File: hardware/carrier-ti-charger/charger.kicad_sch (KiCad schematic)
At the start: 16 parts, among them J2 J_NTC 100k ENTC-EB-100K4262-02, U4 MAX77757JEFG420+T

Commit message: TI charger
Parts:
- removed C34, C7: 2.2u 25V X7R, Capacitor_SMD:C_0603_1608Metric, symbol Device:C
- removed R37, R6: 6.2k 1%, Resistor_SMD:R_0603_1608Metric, symbol Device:R
- removed R8: 154k 1%, Resistor_SMD:R_0603_1608Metric, symbol Device:R
- removed U4: MAX77757JEFG420+T, carrier:FC2QFN-24_L3.0-W3.0-P0.40_MAX77757, symbol carrier:MAX77757JEFG420
- added C41, C42, C47: 10u 25V X7R, Capacitor_SMD:C_0805_2012Metric, symbol Device:C
- added C43, C44, C46, C50: 100n 50V, Capacitor_SMD:C_0603_1608Metric, symbol Device:C
- added C45: 47n 50V, Capacitor_SMD:C_0603_1608Metric, symbol Device:C
- added C48: 4.7u 16V X5R, Capacitor_SMD:C_0603_1608Metric, symbol Device:C
- added C49: 1n 50V, Capacitor_SMD:C_0603_1608Metric, symbol Device:C
- added Q10, Q12: 2N7002, Package_TO_SOT_SMD:SOT-23, symbol Transistor_FET:2N7002
- added R56: 4.7k 1%, Resistor_SMD:R_0603_1608Metric, symbol Device:R
- added R57, R63: 47k 1%, Resistor_SMD:R_0603_1608Metric, symbol Device:R
- added R58, R62, R64: 100k 1%, Resistor_SMD:R_0603_1608Metric, symbol Device:R
- added R59: 80.6k 1%, Resistor_SMD:R_0603_1608Metric, symbol Device:R
- added R60: 768k 1%, Resistor_SMD:R_0603_1608Metric, symbol Device:R
- added R61: 150R, Resistor_SMD:R_0603_1608Metric, symbol Device:R
- added R67, R68: 1M, Resistor_SMD:R_0603_1608Metric, symbol Device:R
- added TP8: CHG_INT_N, carrier:TestPoint_Pad_D1.5mm, symbol Connector:TestPoint
- added U14: LM73100RPWR, carrier:VQFN-10_L2.0-W2.0-P0.45-HR_LM73100, symbol carrier:LM73100RPW
- added U4: BQ25798RQMR, Package_DFN_QFN:Texas_RQM0029A_VQFN-29_4x4mm_P0.4mm, symbol Battery_Management:BQ25798
- C5: value 2.2u 25V X7R -> 100n 50V; LCSC C415535 -> C14663
- C8: value 100n -> 47n 50V; LCSC C14663 -> C1622
- L1: value 1uH FXL0630-1R0-M -> 2.2uH FXL0630-2R2-M; LCSC C167216 -> C167218
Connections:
- net BAT_TS: now also R59.1, R60.1, U4.16 (TS)
- net CHG_STAT_N: now also U4.1 (STAT)
- net GND: now also C41.2, C42.2, C43.2, C44.2, C46.2, C47.2, C48.2, C49.2, C50.2, Q10.2 (S), Q12.2 (S), R56.2, R58.2, R60.2, R64.2, R68.2, U14.2 (OVLO), U14.4 (PGTH), U14.8 (GND), U14.9 (IMON), U4.10 (ACDRV2), U4.11 (ACDRV1), U4.27 (GND)
- net USB_DN: now also U4.7 (D-)
- net USB_DP: now also U4.6 (D+)
- net USB_VBUS: now also C41.1, C42.1, C43.1, R63.1, U4.2 (VBUS), U4.3 (VBUS), U4.8 (VAC2), U4.9 (VAC1)
- net VBAT: now also C47.1, R61.2, U4.22 (BAT), U4.23 (BAT)
- net VSYS: now also C46.1, U4.25 (SYS); no longer L1.2
- net CHG_BTST renamed CHG_BTST1
- net CHG_BTST1: now also U4.4 (BTST1)
- net CHG_BYP renamed CHG_PMID
- net CHG_PMID: now also C44.1, C50.1, R67.1, U14.5 (IN), U4.29 (PMID)
- net CHG_SW renamed CHG_SW1
- net CHG_SW1: now also U4.28 (SW1)
- new net CHG_BATP: R61.1, U4.18 (BATP)
- new net CHG_BTST2: C45.1, U4.19 (BTST2)
- new net CHG_DIS: U4.13 (~{CE})
- new net CHG_ILIM: R57.2, R58.1, U4.17 (ILIM_HIZ)
- new net CHG_INT_N: R62.2, TP8.1, U4.21 (~{INT})
- new net CHG_PROG: R56.1, U4.20 (PROG)
- new net CHG_REGN: C48.1, R57.1, R59.2, U4.5 (REGN)
- new net CHG_SDRV: C49.1, U4.24 (SDRV)
- new net CHG_SW2: C45.2, L1.2, U4.26 (SW2)
- new net ESP_3V3: R62.1
- new net ESP_5V_D: U14.6 (OUT)
- new net ESP_PMID_EN: Q12.3 (D), R67.2, R68.1, U14.1 (EN/UVLO)
- new net I2C_SCL: U4.14 (SCL)
- new net I2C_SDA: U4.15 (SDA)
- new net SW_EN: Q12.1 (G)
- new net USB_G2: Q10.1 (G), R63.2, R64.1
- new net USB_OK_N: Q10.3 (D)
- no-connect marks 0 -> 4
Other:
- note added: "1 A default charge, ESP32-S3 raises ICHG over I2C, watchdog (40 s) falls back. CE from the thermostat path (CHG_DIS high = charging off). TREG default 120 C."
- note added: "Charger BQ25798, 1S, 5 V USB input"
- note added: "D+/D- BC1.2 on chip, CC has Rd only (USB input sheet). No ship FET: SDRV 1 nF, QON open. PROG 4.7k = 1S, 750 kHz. ILIM_HIZ 3.4 V = 3 A. TS 80.6k/768k: 3/43 C."
- note added: "Display feed in charger mode, from PMID:"
- note added: "Q12: slider on = U14 off, no handover on unplug."
- note added: "Red LED: USB present (Q10). Green LED: STAT, charging."
- note added: "inside the charger's input current limit."
- note removed: "Battery charger (MAX77757)"
- title: Charger MAX77757 -> Charger BQ25798
- moved on the sheet: C10, C11, C33, C35, C5, C6, C9, J2, L1

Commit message: Switch parts (BMP580, TPS259474L) due to stock shortage.
Also, add overvoltage (OVLO) protection.
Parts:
- added C55: 2.2n 50V, Capacitor_SMD:C_0603_1608Metric, symbol Device:C
- added R72: 1.65k, Resistor_SMD:R_0603_1608Metric, symbol Device:R
- added R77: 5.1k, carrier:R_0402_1005Metric_NoSilk, symbol Device:R
- added R78: 1.5k, carrier:R_0402_1005Metric_NoSilk, symbol Device:R
- U14: value LM73100RPWR -> TPS259474LRPWR; symbol carrier:LM73100RPW -> carrier:TPS259474LRPW; LCSC C3210761 -> C2864845
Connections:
- net CHG_PMID: now also R77.1
- net GND: now also C55.2, R72.2, R78.2; no longer U14.2 (OVLO), U14.9 (IMON)
- net U14_DVDT: now reaches U14.7 (DVDT)
- net U14_DVDT: now also C55.1
- new net U14_ILM: R72.1, U14.9 (ILM)
- new net U14_OVLO: R77.2, R78.1, U14.2 (OVLO)
- no-connect marks 4 -> 3

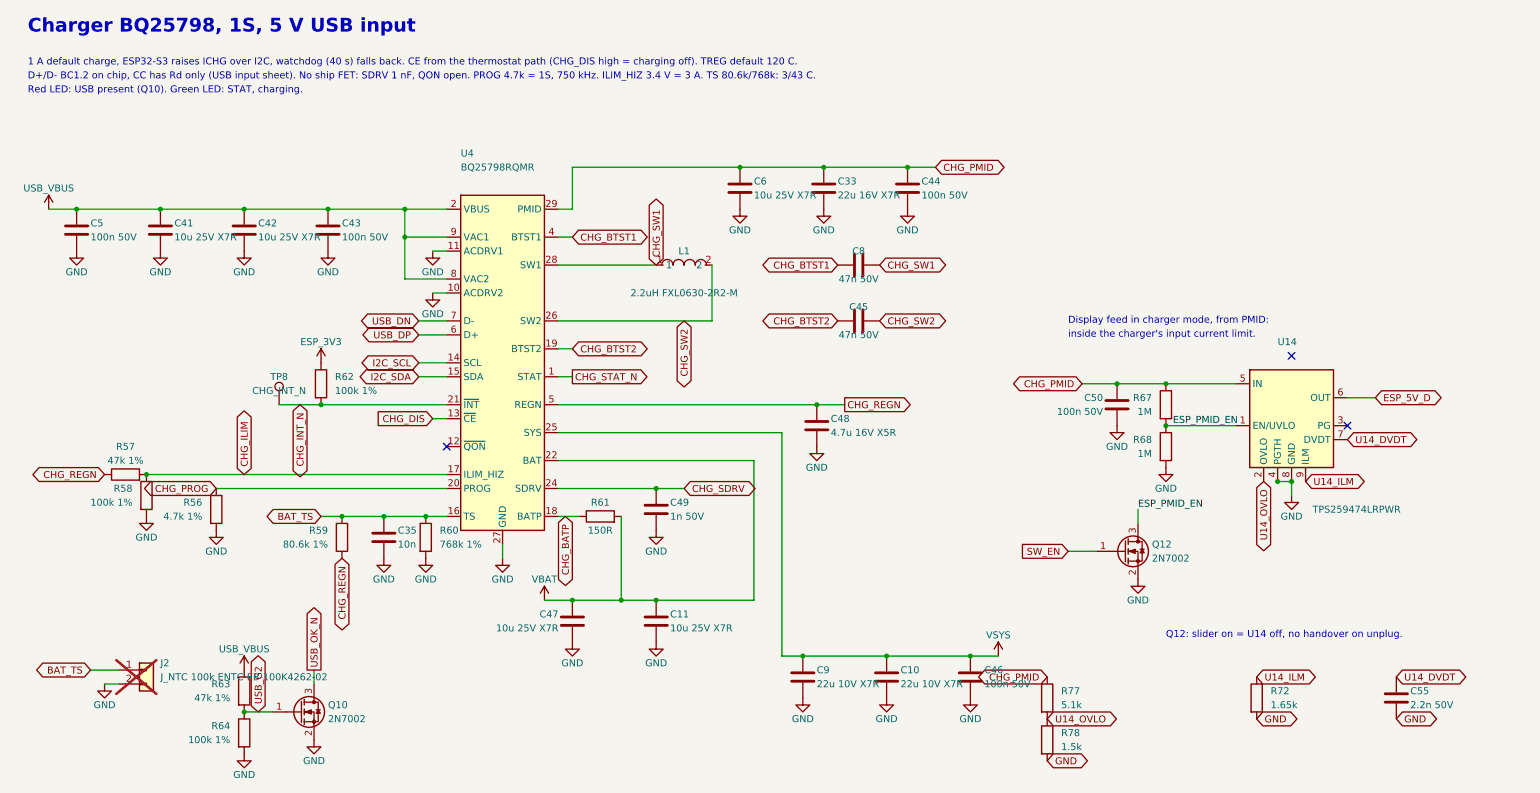
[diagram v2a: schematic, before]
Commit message: Add reset FET switch.
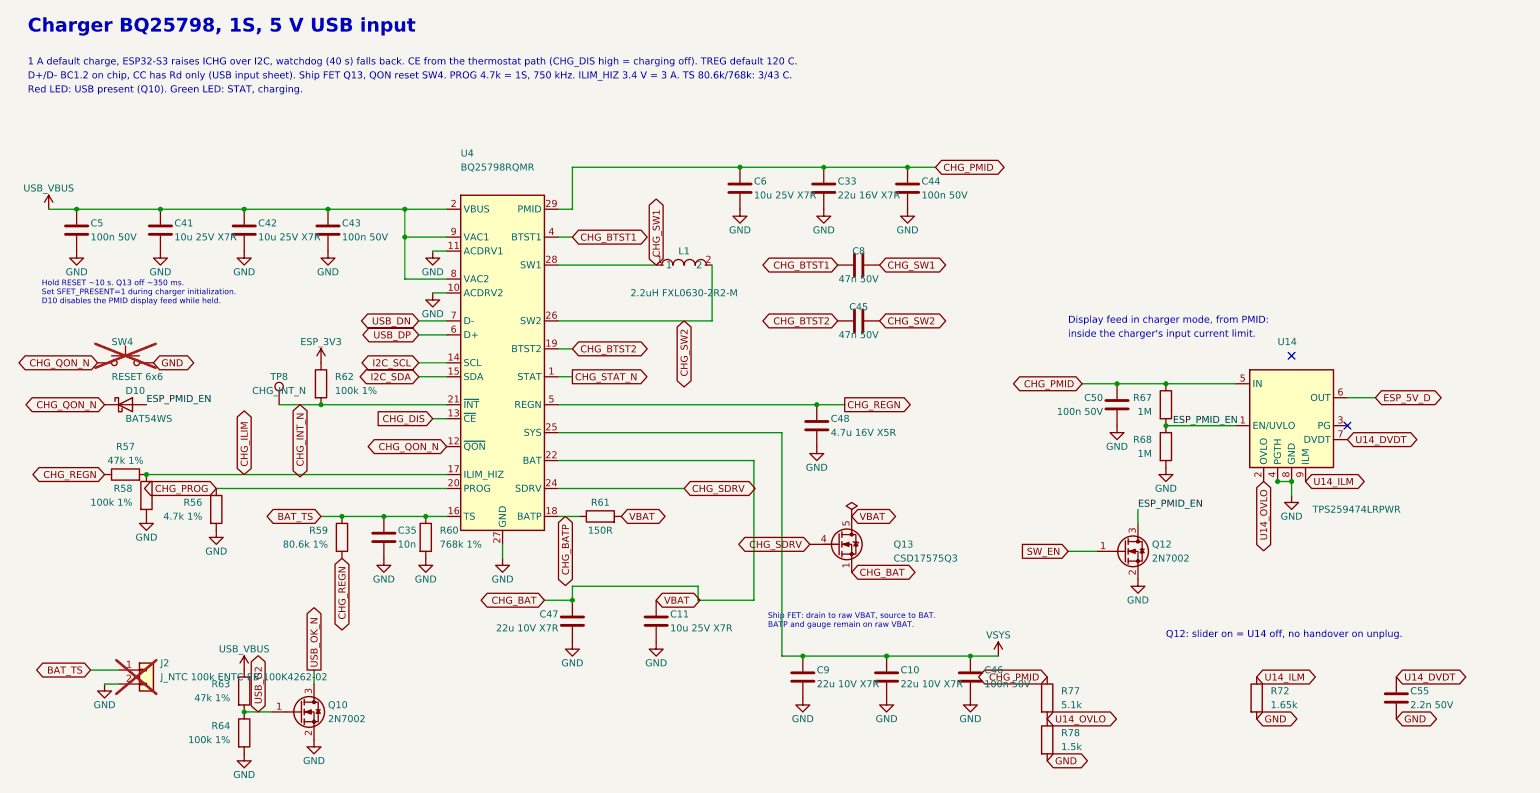
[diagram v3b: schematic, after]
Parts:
- removed C49: 1n 50V, Capacitor_SMD:C_0603_1608Metric, symbol Device:C
- added D10: BAT54WS, Diode_SMD:D_SOD-323, symbol Device:D_Schottky
- added Q13: CSD17575Q3, carrier:VSON-8_3.3x3.3mm_CSD17575Q3, symbol Transistor_FET:Q_NMOS_SSSGD_AvalancheRated
- added SW4: RESET 6x6, Button_Switch_THT:SW_PUSH_6mm, symbol Switch:SW_Push
- C47: value 10u 25V X7R -> 22u 10V X7R; LCSC C3039694 -> C907991
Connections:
- net CHG_SDRV: now also Q13.4 (G)
- net ESP_PMID_EN: now also D10.2 (A)
- net GND: now also SW4.2
- net VBAT: now also Q13.5 (D); no longer C47.1, U4.22 (BAT), U4.23 (BAT)
- net CHG_QON_N: now reaches U4.12 (~{QON})
- net CHG_QON_N: now also D10.1 (K), SW4.1
- new net CHG_BAT: C47.1, Q13.1 (S), Q13.2 (S), Q13.3 (S), U4.22 (BAT), U4.23 (BAT)
- no-connect marks 3 -> 2
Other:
- note added: "D+/D- BC1.2 on chip, CC has Rd only (USB input sheet). Ship FET Q13, QON reset SW4. PROG 4.7k = 1S, 750 kHz. ILIM_HIZ 3.4 V = 3 A. TS 80.6k/768k: 3/43 C."
- note added: "Hold RESET ~10 s. Q13 off ~350 ms. Set SFET_PRESENT=1 during charger initialization. D10 disables the PMID display feed while held."
- note added: "Ship FET: drain to raw VBAT, source to BAT. BATP and gauge remain on raw VBAT."
- note removed: "D+/D- BC1.2 on chip, CC has Rd only (USB input sheet). No ship FET: SDRV 1 nF, QON open. PROG 4.7k = 1S, 750 kHz. ILIM_HIZ 3.4 V = 3 A. TS 80.6k/768k: 3/43 C."

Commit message: Other MH's.
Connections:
- net ESP_3V3 renamed +ESP_3V3
- net ESP_5V_D renamed +ESP_5V_D
- net USB_DN renamed USB_D-
- net USB_DP renamed USB_D+
- net USB_VBUS renamed +VUSB
- net VBAT renamed +VBAT
- net VSYS renamed +VSYS
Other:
- note added: "Ship FET: drain to raw +VBAT, source to BAT. BATP and gauge remain on raw +VBAT."
- note removed: "Ship FET: drain to raw VBAT, source to BAT. BATP and gauge remain on raw VBAT."

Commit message: Update resistors for stock availability.
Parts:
- R77: value 5.1k -> 5.36k; footprint carrier:R_0402_1005Metric_NoSilk -> carrier:R_0805_2012Metric_NoSilk; LCSC C25905 -> C706247; MPN 0402WGF5101TCE -> RT0805BRD075K36L; Manufacturer (none) -> YAGEO; TCR 100 ppm/C -> 25 ppm/C; Tolerance 1% -> 0.1%
- R78: LCSC C25867 -> C281775; MPN 0402WGF1501TCE -> RT0402BRD071K5L; Manufacturer (none) -> YAGEO; TCR 100 ppm/C -> 25 ppm/C; Tolerance 1% -> 0.1%
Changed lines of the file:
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@@
 			)
 		)
-		(property "Datasheet" "https://www.lcsc.com/datasheet/C25867.pdf"
+		(property "Datasheet" "https://datasheet.lcsc.com/datasheet/pdf/46d7760c582640714d605308a25a220a.pdf?productCode=C281775"
 			(at 205.74 151.13 0)
 			(hide yes)
@@
 			)
 		)
-		(property "Description" "OVLO divider, 1%, 100 ppm/C, 62.5 mW, 50 V"
+		(property "Description" "OVLO divider, 0.1%, 25 ppm/C, 62.5 mW, 50 V"
 			(at 205.74 151.13 0)
 			(hide yes)
@@
 			)
 		)
-		(property "LCSC" "C25867"
+		(property "LCSC" "C281775"
 			(at 205.74 151.13 0)
 			(hide yes)
@@
 			)
 		)
-		(property "MPN" "0402WGF1501TCE"
+		(property "MPN" "RT0402BRD071K5L"
 			(at 205.74 151.13 0)
 			(hide yes)
@@
 			)
 		)
-		(property "Tolerance" "1%"
+		(property "Tolerance" "0.1%"
 			(at 205.74 151.13 0)
 			(hide yes)
@@
 			)
 		)
-		(property "TCR" "100 ppm/C"
+		(property "TCR" "25 ppm/C"
+			(at 205.74 151.13 0)
+			(hide yes)
+			(show_name no)
+			(do_not_autoplace no)
+			(effects
+				(font
+					(size 1.27 1.27)
+				)
+			)
+		)
+		(property "Manufacturer" "YAGEO"
 			(at 205.74 151.13 0)
 			(hide yes)
@@
 			)
 		)
-		(property "Value" "5.1k"
+		(property "Value" "5.36k"
 			(at 208.28 144.78 0)
 			(show_name no)
@@
 			)
 		)
-		(property "Footprint" "carrier:R_0402_1005Metric_NoSilk"
+		(property "Footprint" "carrier:R_0805_2012Metric_NoSilk"
 			(at 205.74 143.51 0)
 			(hide yes)
@@
 			)
 		)
-		(property "Datasheet" "https://www.lcsc.com/datasheet/C25905.pdf"
+		(property "Datasheet" "https://datasheet.lcsc.com/datasheet/pdf/46d7760c582640714d605308a25a220a.pdf?productCode=C706247"
 			(at 205.74 143.51 0)
 			(hide yes)
@@
 			)
 		)
-		(property "Description" "OVLO divider, 1%, 100 ppm/C, 62.5 mW, 50 V"
+		(property "Description" "OVLO divider, 0.1%, 25 ppm/C, 125 mW, 150 V"
 			(at 205.74 143.51 0)
 			(hide yes)
@@
 			)
 		)
-		(property "LCSC" "C25905"
+		(property "LCSC" "C706247"
 			(at 205.74 143.51 0)
 			(hide yes)
@@
 			)
 		)
-		(property "MPN" "0402WGF5101TCE"
+		(property "MPN" "RT0805BRD075K36L"
 			(at 205.74 143.51 0)
 			(hide yes)
@@
 			)
 		)
-		(property "Tolerance" "1%"
+		(property "Tolerance" "0.1%"
 			(at 205.74 143.51 0)
 			(hide yes)
@@
 			)
 		)
-		(property "TCR" "100 ppm/C"
+		(property "TCR" "25 ppm/C"
 			(at 205.74 143.51 0)
 			(hide yes)
+			(show_name no)
+			(do_not_autoplace no)
+			(effects
+				(font
+					(size 1.27 1.27)
+				)
+			)
+		)
+		(property "Manufacturer" "YAGEO"
+			(at 205.74 143.51 0)
+			(hide yes)

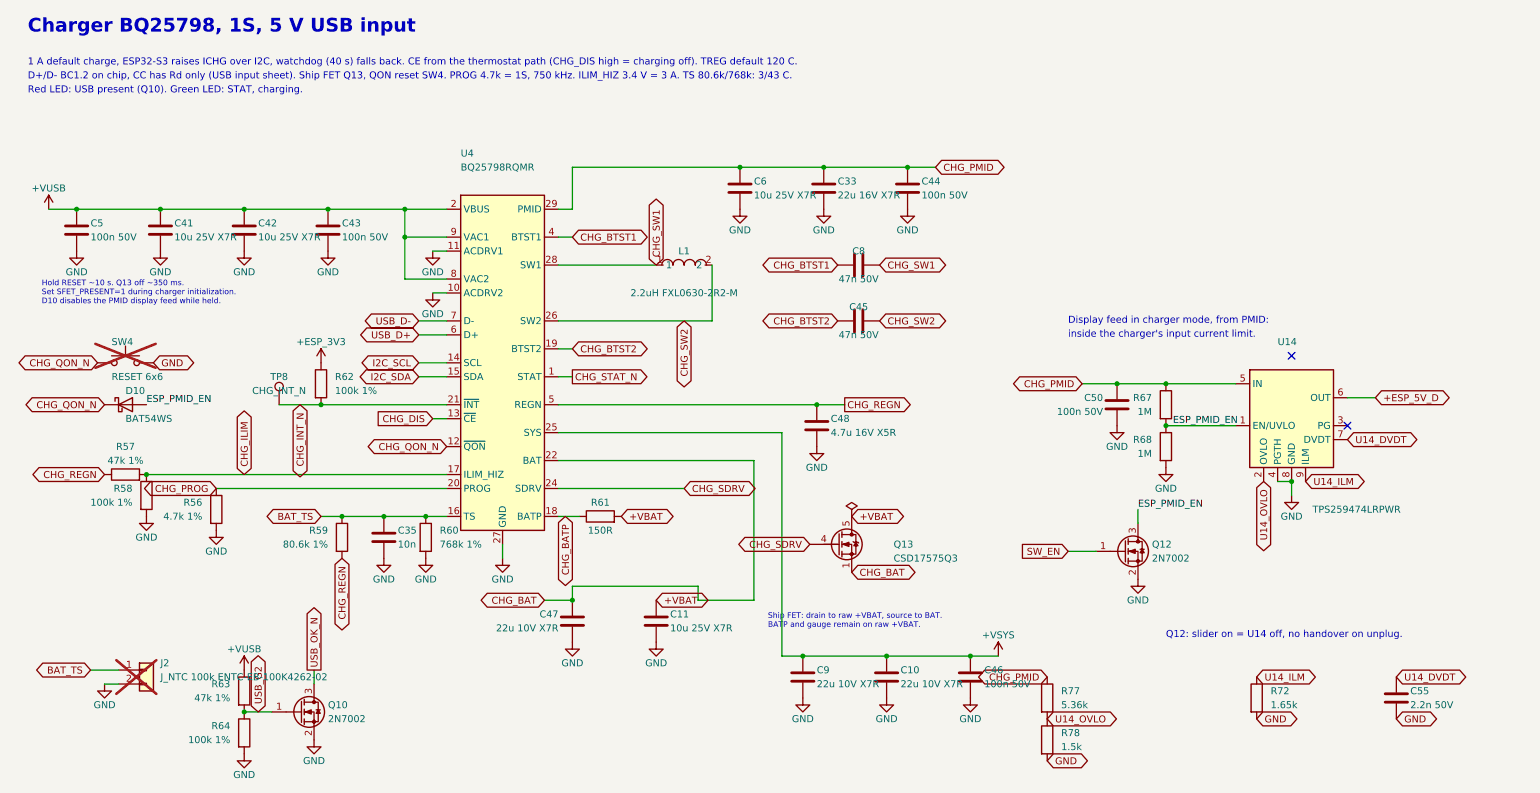
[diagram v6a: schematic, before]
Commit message: Add USB current detection.
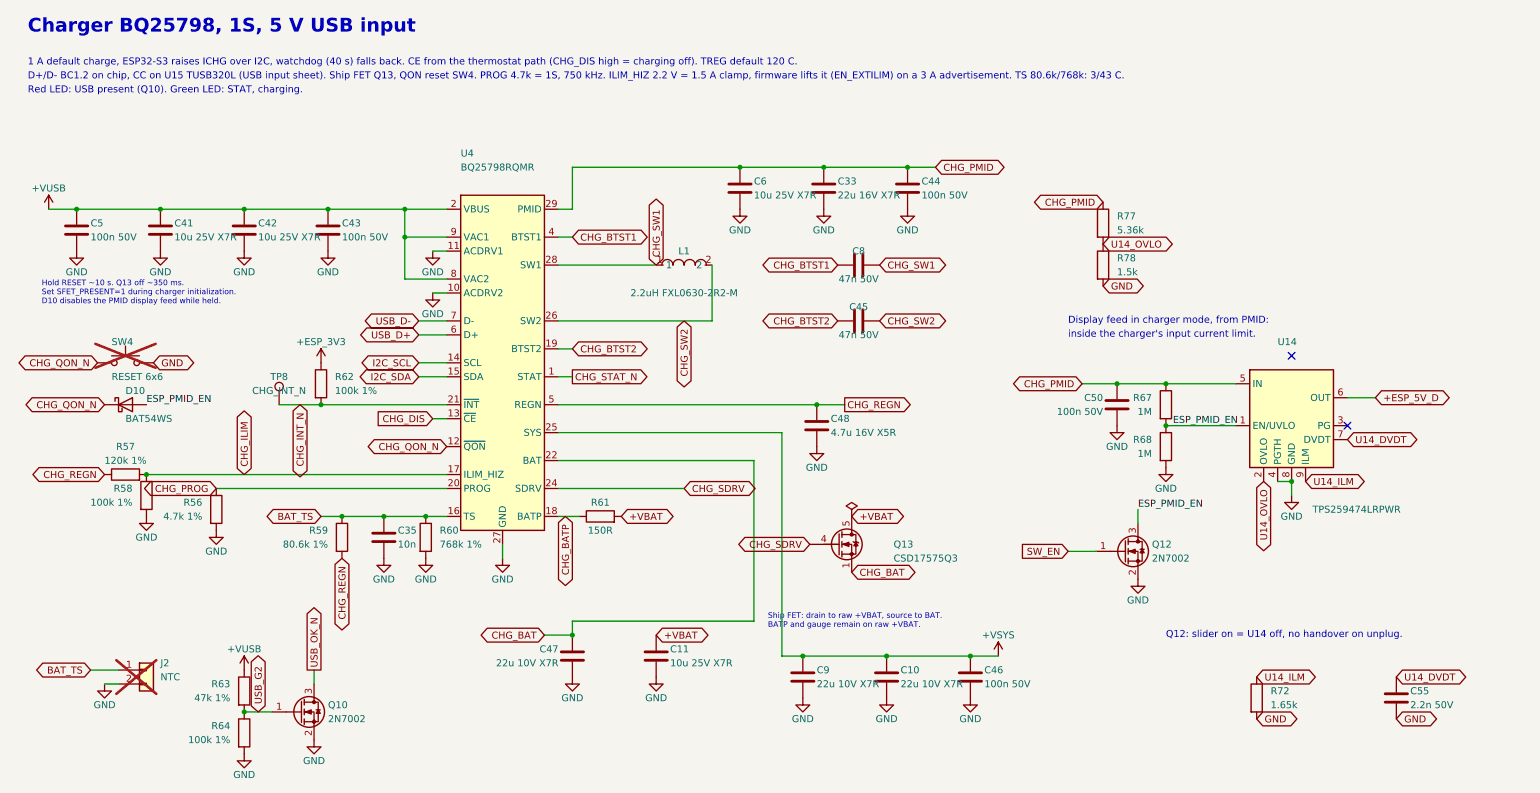
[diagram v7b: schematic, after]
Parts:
- J2: value J_NTC 100k ENTC-EB-100K4262-02 -> NTC
- R57: value 47k 1% -> 120k 1%; LCSC C25819 -> C25808
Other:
- note added: "D+/D- BC1.2 on chip, CC on U15 TUSB320L (USB input sheet). Ship FET Q13, QON reset SW4. PROG 4.7k = 1S, 750 kHz. ILIM_HIZ 2.2 V = 1.5 A clamp, firmware lifts it (EN_EXTILIM) on a 3 A advertisement. TS 80.6k/768k: 3/43 C."
- note removed: "D+/D- BC1.2 on chip, CC has Rd only (USB input sheet). Ship FET Q13, QON reset SW4. PROG 4.7k = 1S, 750 kHz. ILIM_HIZ 3.4 V = 3 A. TS 80.6k/768k: 3/43 C."
- moved on the sheet: C11, C47, R77, R78
